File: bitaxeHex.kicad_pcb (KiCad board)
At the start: 4 copper layers, 84.5 x 129.5 mm, 369 parts, among them J1 XT30, J3 Conn_02x05_Odd_Even, J4 TC2030-IDC, J5 Conn_01x04, J6 Conn_01x06, J7 USB_C_Receptacle_USB2.0, J8 Conn_01x04, J9 Conn_01x04, SW1 SWITCH-SPST, SW2 SWITCH-SPST, U1 LMR54410, U10 SGM2036-0v8, U11 SGM2036-1v8, U12 BM1366_mode1, U13 BM1366_mode1, U14 25MHz, U15 TLV3544, U16 SGM2036-1v8, U17 SGM2036-0v8, U18 BM1366_mode0, U19 25MHz, U2 RT9080-33GJ5, U20 BM1366_mode0, U21 TLV3544, U22 BM1366_mode1, U23 SGM2036-0v8, U24 SGM2036-1v8, U25 BM1366_mode1, U26 25MHz, U3 TPS546D24ARVFR, U4 MIC5504, U5 SN74AVC4T774, U6 ESP32-S3-WROOM-1, U7 TMP1075, U8 TMP1075, U9 EMC2302, Y1 32.768kHz

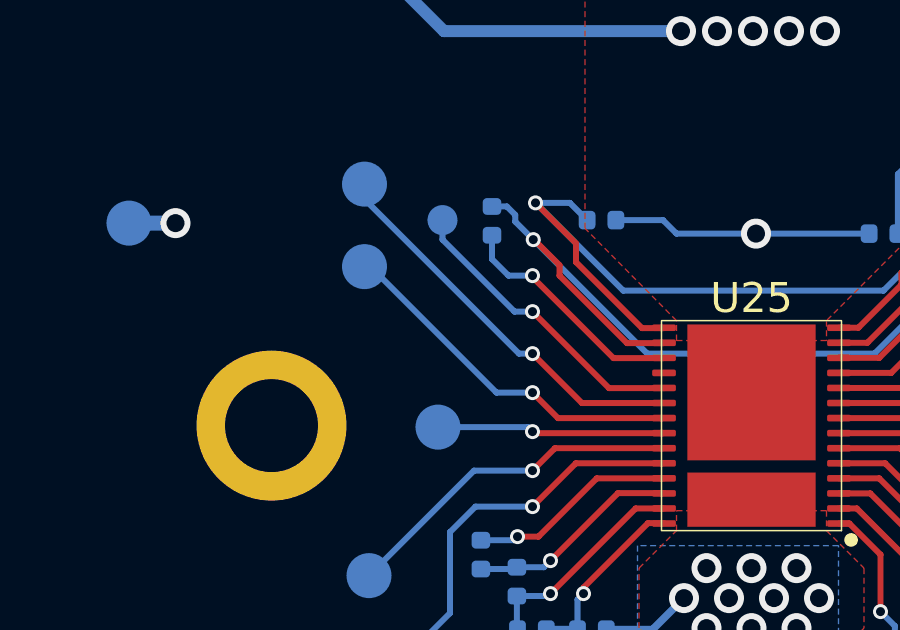
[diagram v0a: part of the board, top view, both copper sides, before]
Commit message: Issues about the RI pull-up resistor at the end of the chip chain being fixed
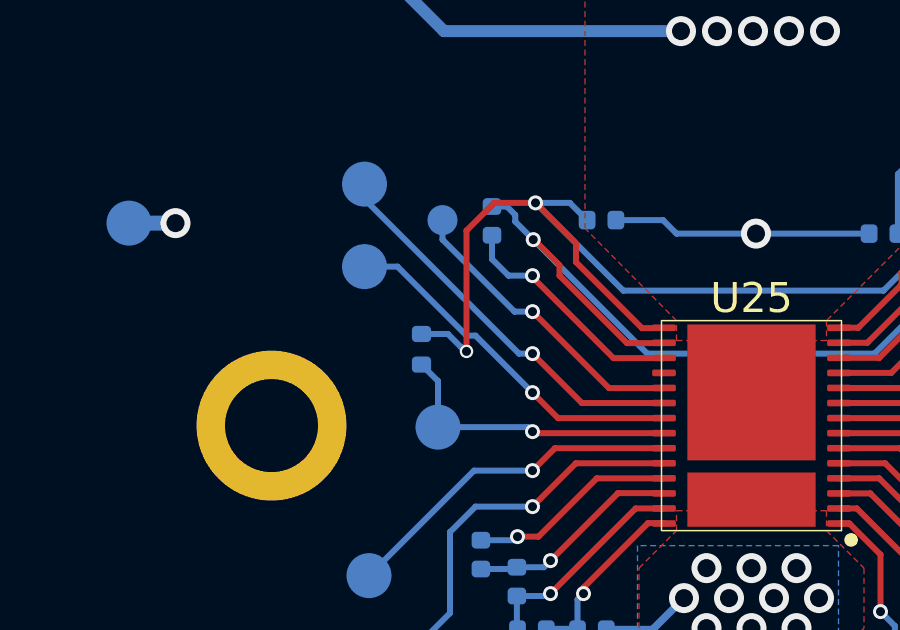
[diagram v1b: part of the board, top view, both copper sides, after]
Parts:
- added R80: 10k, Resistor_SMD:R_0402_1005Metric, B.Cu at (67.0, 150.5)
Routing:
- net /BM1366-3/1V8: track 98.4 -> 106.8 mm, vias 4 -> 5
- net /BM1366-3/RI3: track 7.62 -> 9.93 mm
